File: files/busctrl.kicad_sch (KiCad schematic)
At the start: 3 parts, among them J1 VLB_slot, U2 27C010

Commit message: work on the memory bus, fixed symbols
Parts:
- removed J1: VLB_slot, symbol virge:VLB_slot
- removed U?: 86C375_layout, Package_QFP:PQFP-208_28x28mm_P0.5mm, symbol virge:86C375_layout
- added J1: VLB_slot, VLB:BUS_VLB_Board, symbol virge:VLB_slot
- U2: footprint (none) -> Package_DIP:DIP-32_W15.24mm
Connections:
- net +5V: now also J1.C29 (VCC), J1.C3 (VCC)
- net -12V: now also J1.C7 (-12V)
- net A0: now also J1.C62 (BA00)
- net A1: now also J1.C61 (BA01)
- net A10: now also J1.C52 (BA10)
- net A11: now also J1.C51 (BA11)
- net A12: now also J1.C50 (BA12)
- net A13: now also J1.C49 (BA13)
- net A14: now also J1.C48 (BA14)
- net A15: now also J1.C47 (BA15)
- net A16: now also J1.C46 (BA16)
- net A2: now also J1.C60 (BA02)
- net A3: now also J1.C59 (BA03)
- net A4: now also J1.C58 (BA04)
- net A5: now also J1.C57 (BA05)
- net A6: now also J1.C56 (BA06)
- net A7: now also J1.C55 (BA07)
- net A8: now also J1.C54 (BA08)
- net A9: now also J1.C53 (BA09)
- net D0: now also J1.C40 (DB0)
- net D1: now also J1.C39 (DB1)
- net D2: now also J1.C38 (DB2)
- net D3: now also J1.C37 (DB3)
- net D4: now also J1.C36 (DB4)
- net D5: now also J1.C35 (DB5)
- net D6: now also J1.C34 (DB6)
- net D7: now also J1.C33 (DB7)
- net GND: now also J1.C1 (GND), J1.C10 (GND), J1.C31 (GND)
- net at U2.24 (~{OE}): now also J1.C12 (~{SMEMR})

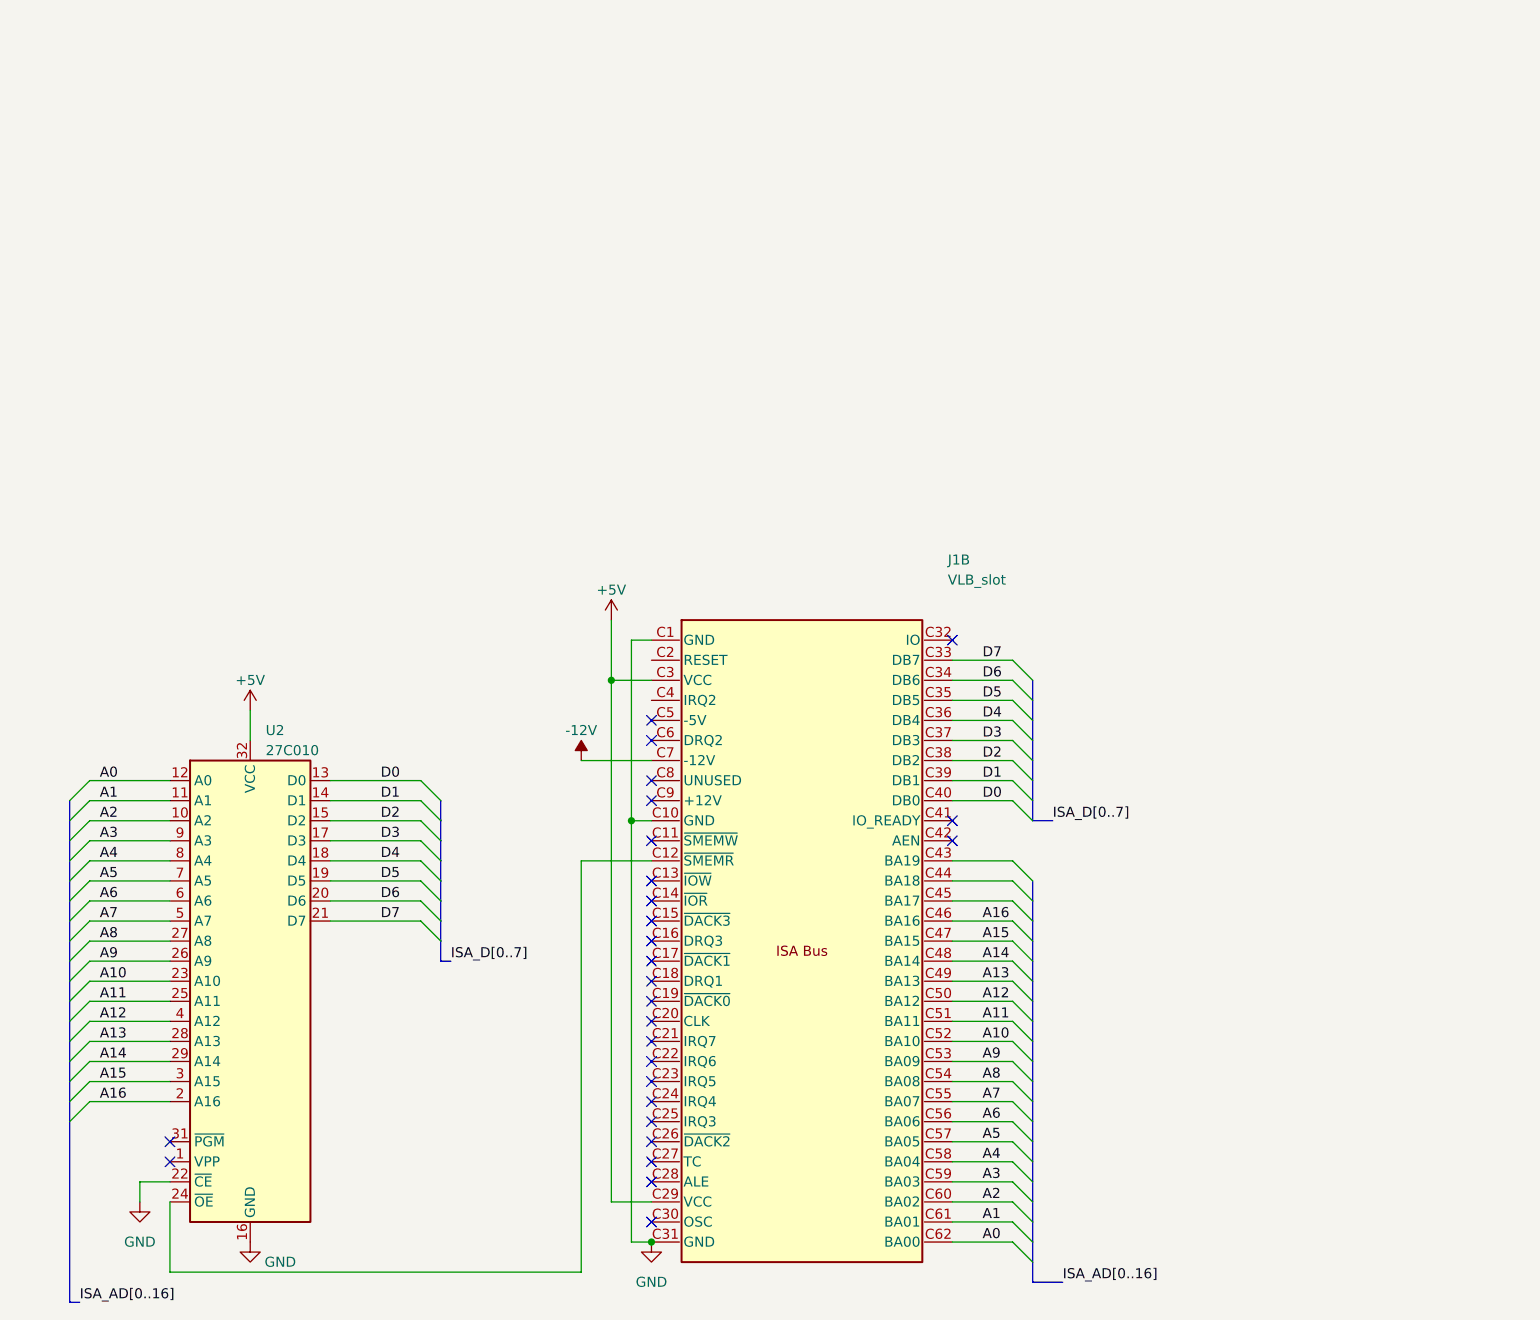
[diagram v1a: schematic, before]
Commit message: changed memory chips, more progress
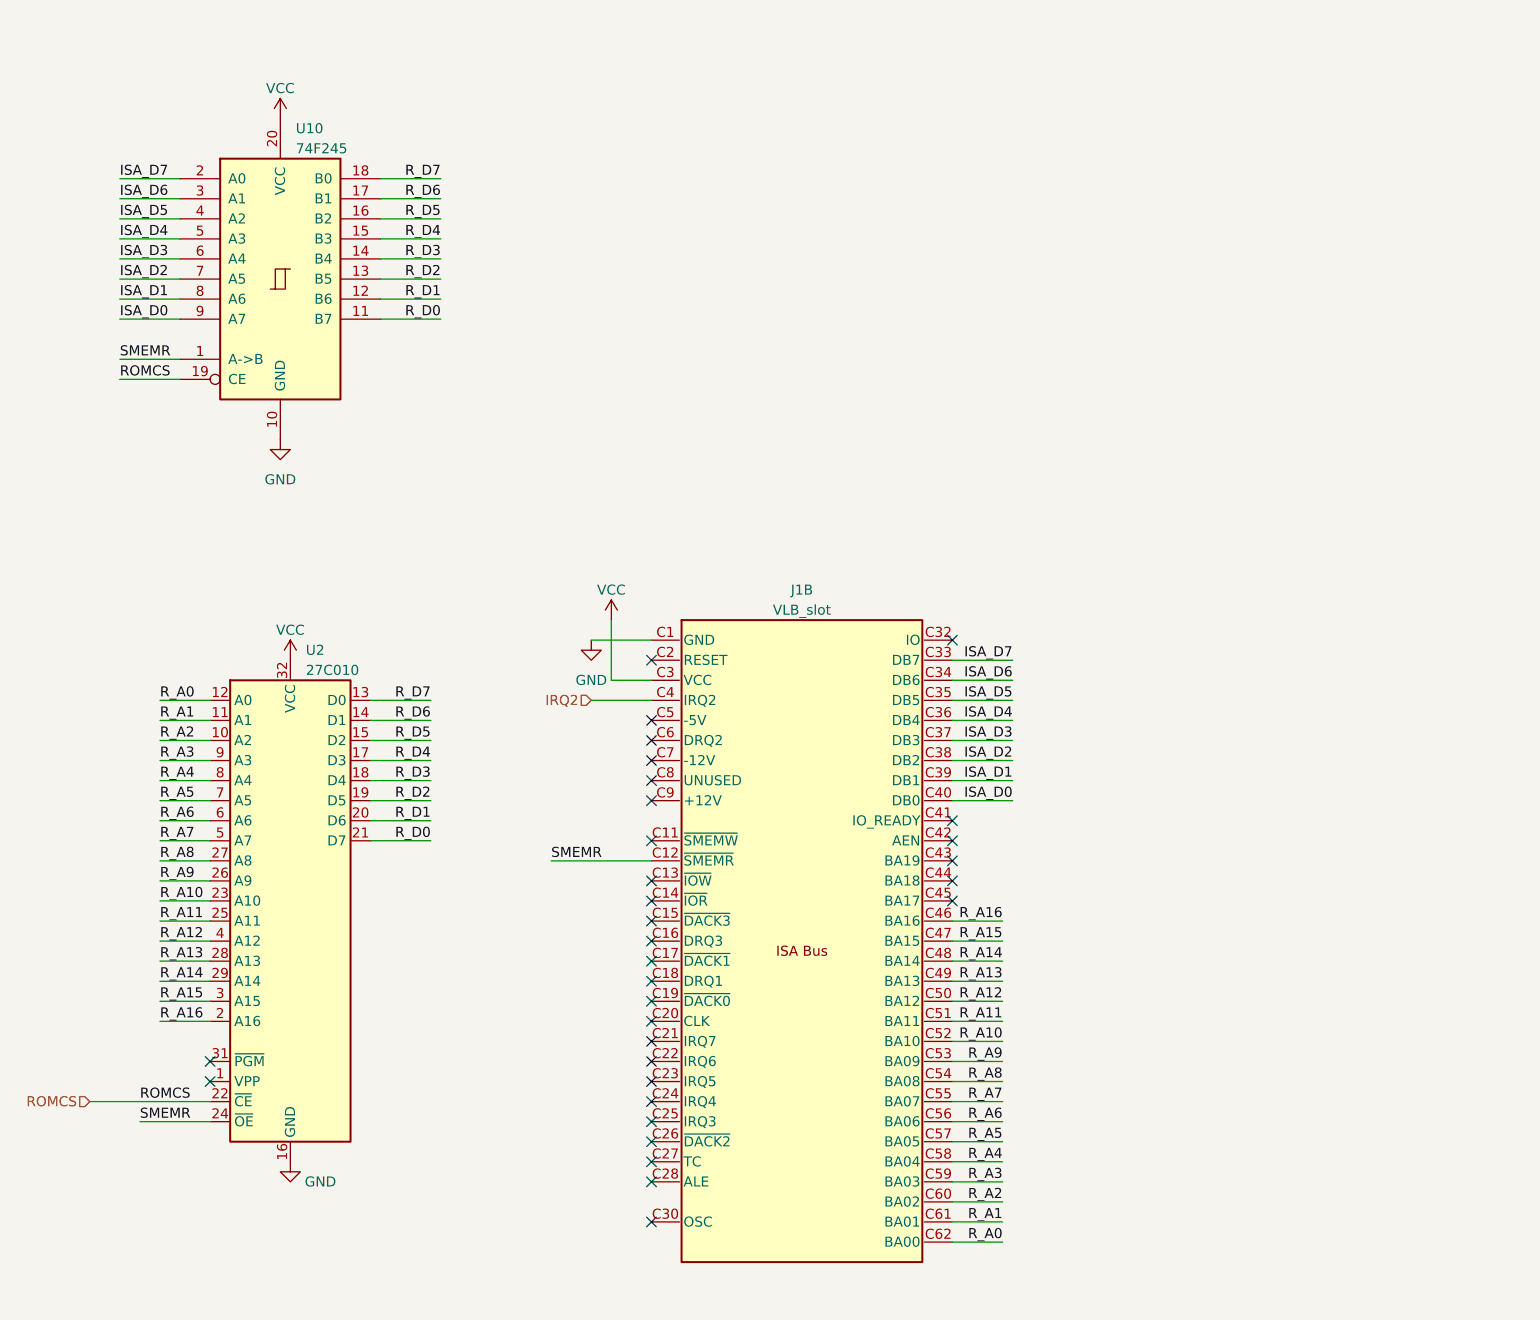
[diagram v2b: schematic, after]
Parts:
- added U10: 74F245, Package_SO:SO-20_5.3x12.6mm_P1.27mm, symbol 74xx:74LS245
- J1: footprint VLB:BUS_VLB_Board -> (none)
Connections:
- net GND: now also U10.10 (GND); no longer U2.22 (~{CE})
- net SMEMR: now reaches J1.C12 (~{SMEMR}), U2.24 (~{OE})
- net SMEMR: now also U10.1 (A->B)
- net IRQ2: now reaches J1.C4 (IRQ2)
- net +5V renamed VCC
- net VCC: now also U10.20 (VCC)
- net -12V: no longer names the net of J1.C7 (-12V)
- net A0 renamed R_A0
- net A1 renamed R_A1
- net A10 renamed R_A10
- net A11 renamed R_A11
- net A12 renamed R_A12
- net A13 renamed R_A13
- net A14 renamed R_A14
- net A15 renamed R_A15
- net A16 renamed R_A16
- net A2 renamed R_A2
- net A3 renamed R_A3
- net A4 renamed R_A4
- net A5 renamed R_A5
- net A6 renamed R_A6
- net A7 renamed R_A7
- net A8 renamed R_A8
- net A9 renamed R_A9
- net D0 renamed ISA_D0
- net ISA_D0: now also U10.9 (A7); no longer U2.13 (D0)
- net D1 renamed ISA_D1
- net ISA_D1: now also U10.8 (A6); no longer U2.14 (D1)
- net D2 renamed ISA_D2
- net ISA_D2: now also U10.7 (A5); no longer U2.15 (D2)
- net D3 renamed ISA_D3
- net ISA_D3: now also U10.6 (A4); no longer U2.17 (D3)
- net D4 renamed ISA_D4
- net ISA_D4: now also U10.5 (A3); no longer U2.18 (D4)
- net D5 renamed ISA_D5
- net ISA_D5: now also U10.4 (A2); no longer U2.19 (D5)
- net D6 renamed ISA_D6
- net ISA_D6: now also U10.3 (A1); no longer U2.20 (D6)
- net D7 renamed ISA_D7
- net ISA_D7: now also U10.2 (A0); no longer U2.21 (D7)
- new net ROMCS: U10.19 (CE), U2.22 (~{CE})
- new net R_D0: U10.11 (B7), U2.21 (D7)
- new net R_D1: U10.12 (B6), U2.20 (D6)
- new net R_D2: U10.13 (B5), U2.19 (D5)
- new net R_D3: U10.14 (B4), U2.18 (D4)
- new net R_D4: U10.15 (B3), U2.17 (D3)
- new net R_D5: U10.16 (B2), U2.15 (D2)
- new net R_D6: U10.17 (B1), U2.14 (D1)
- new net R_D7: U10.18 (B0), U2.13 (D0)
- no-connect marks 27 -> 32
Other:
- moved on the sheet: U2

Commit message: PCB work
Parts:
- J1: footprint (none) -> VLB:BUS_VLB_Board
- U10: value 74F245 -> 74LS245; footprint Package_SO:SO-20_5.3x12.6mm_P1.27mm -> Package_DIP:DIP-20_W7.62mm
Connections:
- net R_D0: now also U2.13 (D0); no longer U2.21 (D7)
- net R_D1: now also U2.14 (D1); no longer U2.20 (D6)
- net R_D2: now also U2.15 (D2); no longer U2.19 (D5)
- net R_D3: now also U2.17 (D3); no longer U2.18 (D4)
- net R_D4: now also U2.18 (D4); no longer U2.17 (D3)
- net R_D5: now also U2.19 (D5); no longer U2.15 (D2)
- net R_D6: now also U2.20 (D6); no longer U2.14 (D1)
- net R_D7: now also U2.21 (D7); no longer U2.13 (D0)

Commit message: initial PCB routed
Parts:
- removed U2: 27C010, Package_DIP:DIP-32_W15.24mm, symbol Memory_EPROM:27C010
- added R32 (x2): 0R, Resistor_SMD:R_0805_2012Metric_Pad1.20x1.40mm_HandSolder, symbol Device:R
- added U2: 27C020, Package_DIP:DIP-32_W15.24mm, symbol Memory_EPROM:27C020
- U10: footprint Package_DIP:DIP-20_W7.62mm -> Package_SO:SO-20_5.3x12.6mm_P1.27mm
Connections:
- net GND: now also U2.16 (GND)
- net ROMCS: now also U2.22 (~{CE})
- net R_A0: now also U2.12 (A0)
- net R_A1: now also U2.11 (A1)
- net R_A10: now also U2.23 (A10)
- net R_A11: now also U2.25 (A11)
- net R_A12: now also U2.4 (A12)
- net R_A13: now also U2.28 (A13)
- net R_A14: now also U2.29 (A14)
- net R_A15: now also U2.3 (A15)
- net R_A2: now also U2.10 (A2)
- net R_A3: now also U2.9 (A3)
- net R_A4: now also U2.8 (A4)
- net R_A5: now also U2.7 (A5)
- net R_A6: now also U2.6 (A6)
- net R_A7: now also U2.5 (A7)
- net R_A8: now also U2.27 (A8)
- net R_A9: now also U2.26 (A9)
- net R_D0: now also U2.13 (D0)
- net R_D1: now also U2.14 (D1)
- net R_D2: now also U2.15 (D2)
- net R_D3: now also U2.17 (D3)
- net R_D4: now also U2.18 (D4)
- net R_D5: now also U2.19 (D5)
- net R_D6: now also U2.20 (D6)
- net R_D7: now also U2.21 (D7)
- net SMEMR: now also U2.24 (~{OE})
- net VCC: now also R32.2, R32.2, U2.32 (VCC)
- net IRQ2: no longer names the net of J1.C4 (IRQ2)
- new net: R32.1, U2.2 (A16)
- new net: R32.1, U2.30 (A17)
- no-connect marks 32 -> 33
